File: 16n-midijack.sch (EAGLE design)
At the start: 108 parts, among them J1 PJ302M, J10 PJ302M, J11 PJ302M, J12 PJ302M, J13 PJ302M, J14 PJ302M, J15 PJ302M, J16 PJ302M, J2 PJ302M, J3 PJ302M, J4 PJ302M, J5 PJ302M, J6 PJ302M, J7 PJ302M, J8 PJ302M, J9 PJ302M, U1 MCP6004_SMD, U2 MCP6004_SMD, U3 MCP6004_SMD, U4 MCP6004_SMD, U5 MCP6004_SMD, U6 MCP6004_SMD, U7 MCP6004_SMD, U8 MCP6004_SMD

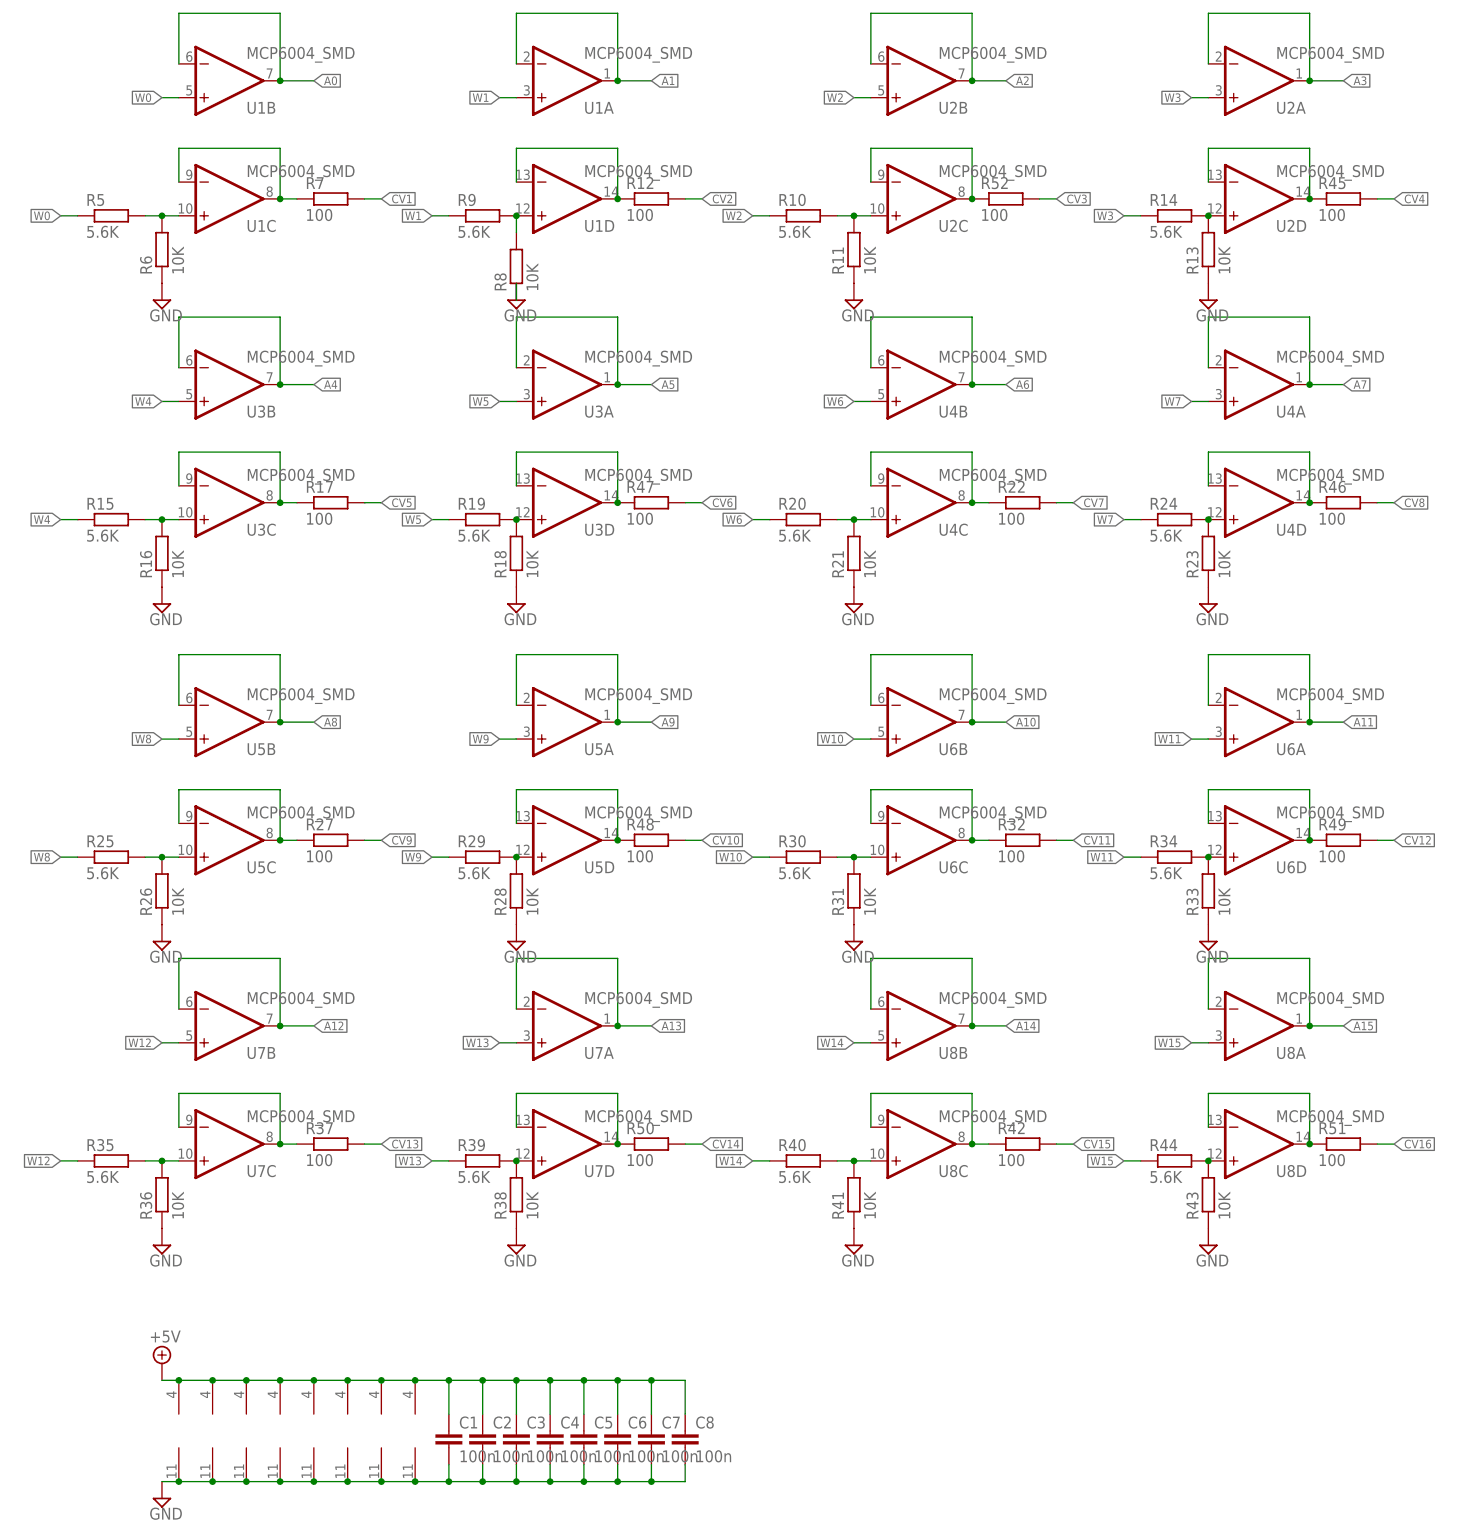
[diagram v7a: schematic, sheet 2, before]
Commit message: Correcting outputs.
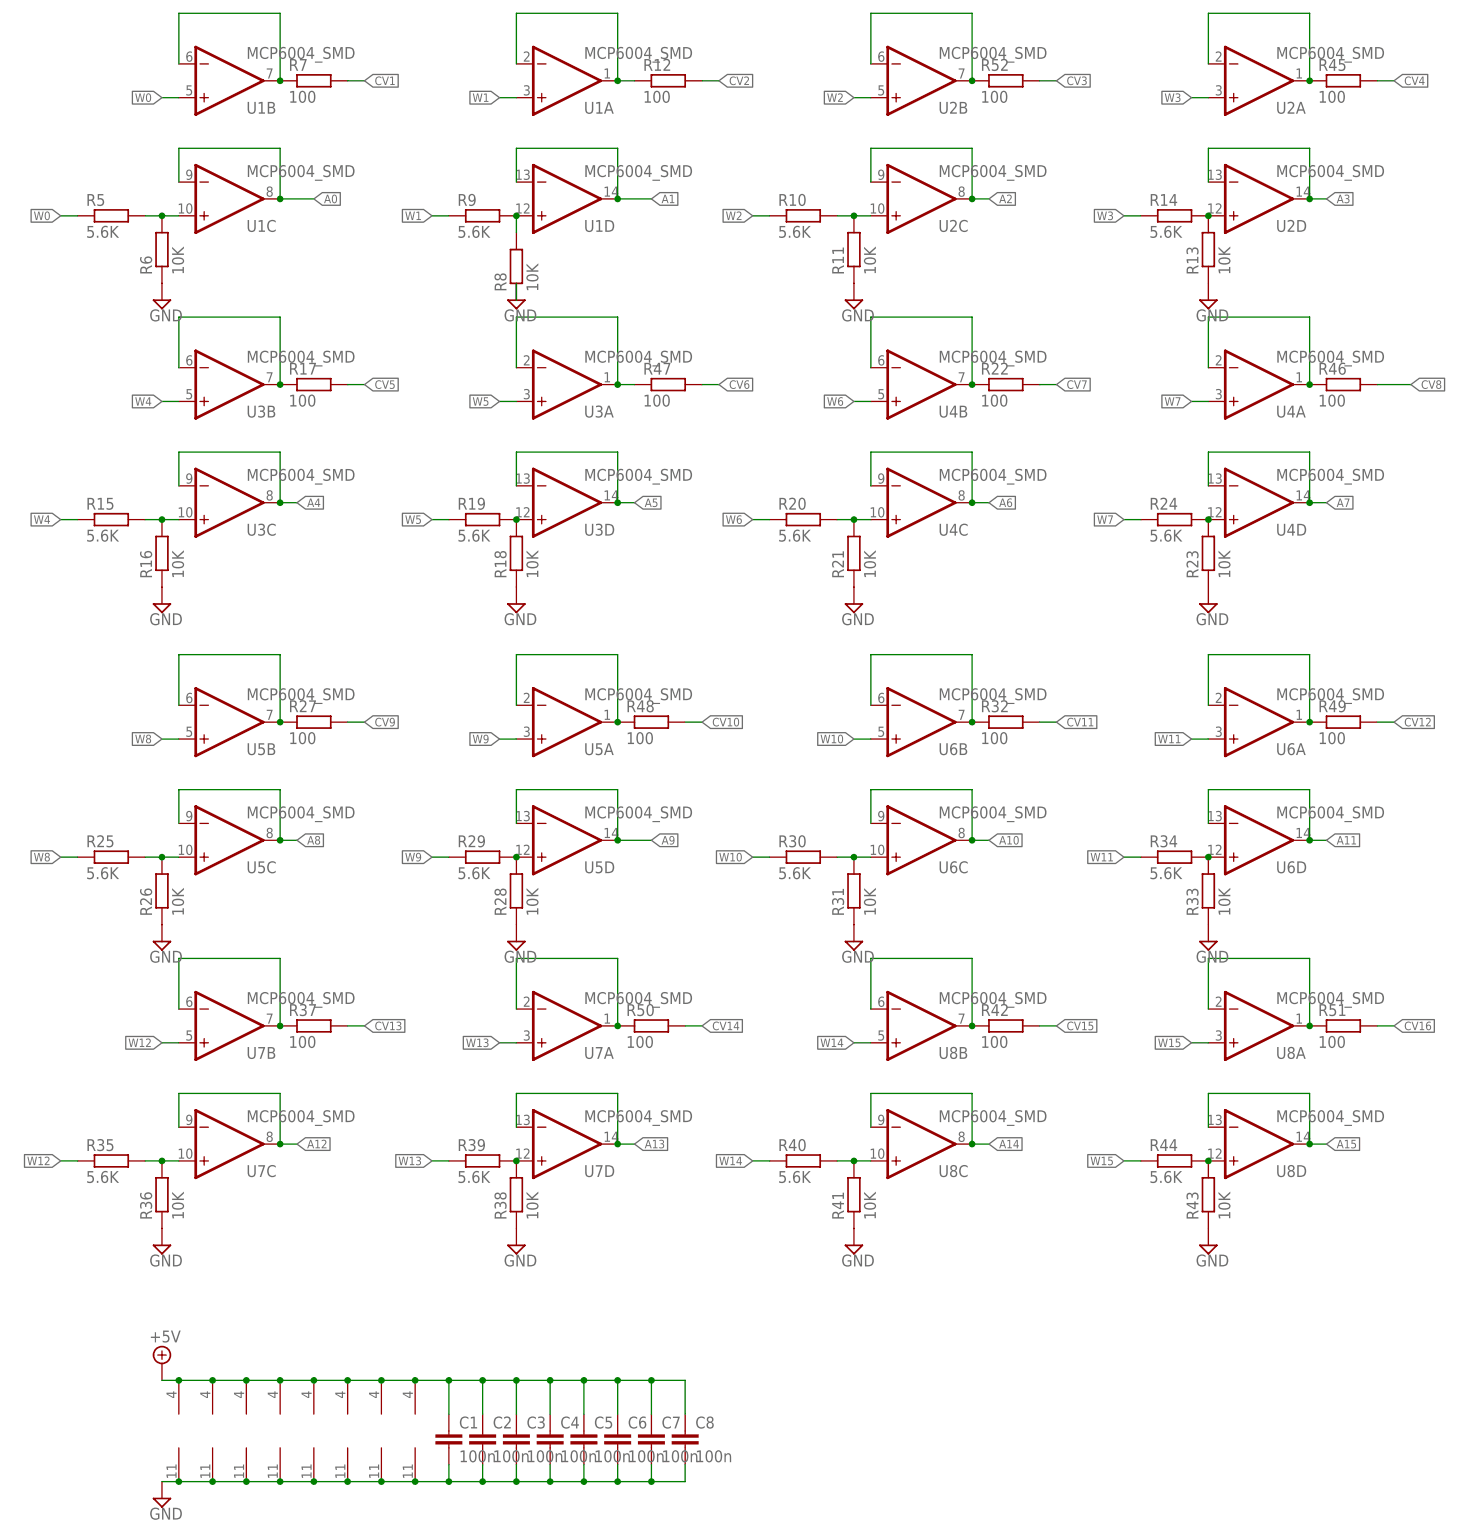
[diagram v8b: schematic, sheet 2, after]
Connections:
- removed net N$11: R17.1, U3C.-IN, U3C.OUT
- removed net N$14: R22.1, U4C.-IN, U4C.OUT
- removed net N$17: R27.1, U5C.-IN, U5C.OUT
- removed net N$20: R32.1, U6C.-IN, U6C.OUT
- removed net N$23: R37.1, U7C.-IN, U7C.OUT
- removed net N$256: R12.1, U1D.-IN, U1D.OUT
- removed net N$257: R45.1, U2D.-IN, U2D.OUT
- removed net N$258: R47.1, U3D.-IN, U3D.OUT
- removed net N$259: R46.1, U4D.-IN, U4D.OUT
- removed net N$26: R42.1, U8C.-IN, U8C.OUT
- removed net N$260: R48.1, U5D.-IN, U5D.OUT
- removed net N$261: R49.1, U6D.-IN, U6D.OUT
- removed net N$262: R50.1, U7D.-IN, U7D.OUT
- removed net N$263: R51.1, U8D.-IN, U8D.OUT
- removed net N$5: R52.1, U2C.-IN, U2C.OUT
- removed net N$8: R7.1, U1C.-IN, U1C.OUT
- net A0: now also R7.1, U1C.-IN, U1C.OUT
- net A1: now also R12.1, U1D.-IN, U1D.OUT
- net A10: now also R32.1, U6C.-IN, U6C.OUT
- net A11: now also R49.1, U6D.-IN, U6D.OUT
- net A12: now also R37.1, U7C.-IN, U7C.OUT
- net A13: now also R50.1, U7D.-IN, U7D.OUT
- net A14: now also R42.1, U8C.-IN, U8C.OUT
- net A15: now also R51.1, U8D.-IN, U8D.OUT
- net A2: now also R52.1, U2C.-IN, U2C.OUT
- net A3: now also R45.1, U2D.-IN, U2D.OUT
- net A4: now also R17.1, U3C.-IN, U3C.OUT
- net A5: now also R47.1, U3D.-IN, U3D.OUT
- net A6: now also R22.1, U4C.-IN, U4C.OUT
- net A7: now also R46.1, U4D.-IN, U4D.OUT
- net A8: now also R27.1, U5C.-IN, U5C.OUT
- net A9: now also R48.1, U5D.-IN, U5D.OUT
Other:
- moved on the sheet: R12, R17, R22, R27, R32, R37, R42, R45, R46, R47, R48, R49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
